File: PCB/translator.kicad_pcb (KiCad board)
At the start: 4 copper layers, 28.2 x 16 mm, 10 parts, among them J1 Conn_01x04_Pin, J2 Conn_01x04_Pin, J3 Conn_01x03_Pin, J4 Conn_01x03_Pin, SW1 SW_Push, U1 STM32G071GBU6

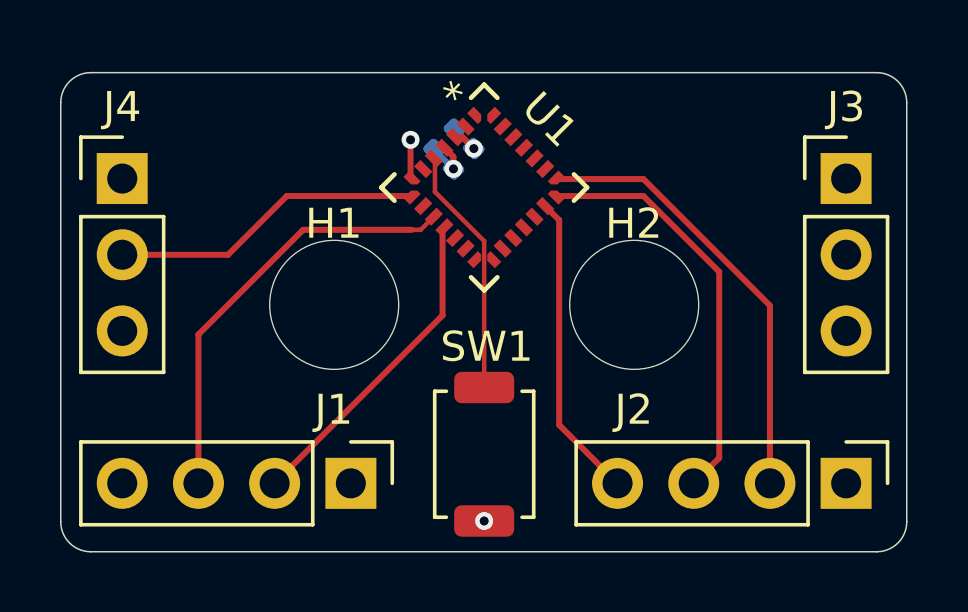
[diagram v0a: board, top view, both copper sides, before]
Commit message: reorganize and add CAD
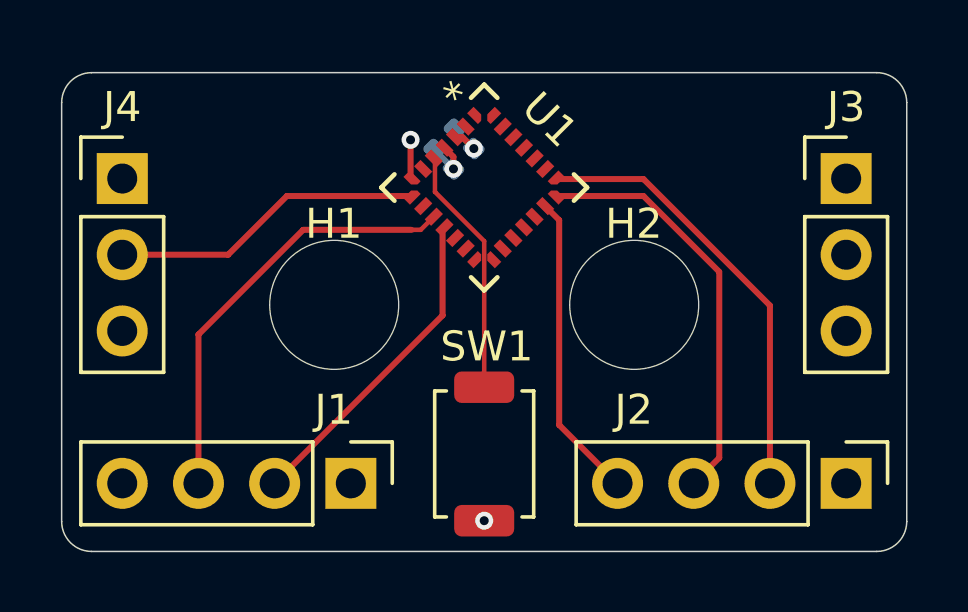
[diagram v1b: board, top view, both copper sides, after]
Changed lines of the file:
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@@
 	(footprint "Button_Switch_SMD:SW_SPST_TS-1088-xR020"
 		(layer "F.Cu")
-		(at 107.315 108.25 90)
+		(at 107.315 108.24 90)
 		(descr "SMD Tactile Switch, 3.9x3x2 mm, https://lcsc.com/datasheet/lcsc_datasheet_2504101957_XUNPU-TS-1088-AR02016_C720477.pdf")
 		(tags "Tactile Switch")
@@
 	)
 	(gr_line
-		(start 93.2 96.53)
-		(end 93.2 110.5)
+		(start 93.23 96.53)
+		(end 93.23 110.49)
 		(stroke
 			(width 0.05)
@@
 	)
 	(gr_arc
-		(start 93.2 96.53)
-		(mid 93.492893 95.822893)
-		(end 94.2 95.53)
+		(start 93.23 96.53)
+		(mid 93.522893 95.822893)
+		(end 94.23 95.53)
 		(stroke
 			(width 0.05)
@@
 	)
 	(gr_arc
-		(start 94.2 111.5)
-		(mid 93.492893 111.207107)
-		(end 93.2 110.5)
+		(start 94.23 111.49)
+		(mid 93.522893 111.197107)
+		(end 93.23 110.49)
 		(stroke
 			(width 0.05)
@@
 	(gr_line
 		(start 120.4 95.53)
-		(end 94.2 95.53)
+		(end 94.23 95.53)
 		(stroke
 			(width 0.05)
@@
 	)
 	(gr_line
-		(start 120.4 111.5)
-		(end 94.2 111.5)
+		(start 120.4 111.49)
+		(end 94.23 111.49)
 		(stroke
 			(width 0.05)
@@
 	)
 	(gr_arc
-		(start 121.4 110.5)
-		(mid 121.107107 111.207107)
-		(end 120.4 111.5)
+		(start 121.4 110.49)
+		(mid 121.107107 111.197107)
+		(end 120.4 111.49)
 		(stroke
 			(width 0.05)
@@
 	)
 	(gr_line
-		(start 121.4 110.5)
+		(start 121.4 110.49)
 		(end 121.4 96.53)
 		(stroke
@@
 	)
 	(via
-		(at 107.315 110.475)
+		(at 107.315 110.465)
 		(size 0.6)
 		(drill 0.3)
@@
 	)
 	(segment
-		(start 106.06 109.22)
-		(end 107.315 110.475)
+		(start 113.300589 98.060589)
+		(end 119.38 104.14)
 		(width 0.2)
 		(layer "In2.Cu")
@@
 	)
 	(segment
-		(start 113.300589 98.060589)
-		(end 119.38 104.14)
+		(start 109.71 108.07)
+		(end 107.315 110.465)
 		(width 0.2)
 		(layer "In2.Cu")
@@
 	)
 	(segment
-		(start 107.315 110.475)
-		(end 109.72 108.07)
+		(start 118.23 108.07)
+		(end 109.71 108.07)
 		(width 0.2)
 		(layer "In2.Cu")
@@
 	)
 	(segment
-		(start 109.72 108.07)
-		(end 118.23 108.07)
+		(start 102.87 109.22)
+		(end 97.79 104.14)
 		(width 0.2)
 		(layer "In2.Cu")
@@
 	)
 	(segment
-		(start 102.87 109.22)
-		(end 97.79 104.14)
+		(start 106.07 109.22)
+		(end 107.315 110.465)
 		(width 0.2)
 		(layer "In2.Cu")
@@
 	(segment
 		(start 102.87 109.22)
-		(end 106.06 109.22)
+		(end 106.07 109.22)
 		(width 0.2)
 		(layer "In2.Cu")
@@
 	)
 	(segment
-		(start 118.23 108.07)
-		(end 119.38 109.22)
+		(start 119.38 109.22)
+		(end 118.23 108.07)
 		(width 0.2)
 		(layer "In2.Cu")
@@
 	)
 	(segment
+		(start 107.315 101.145442)
+		(end 107.315 106.015)
+		(width 0.15)
+		(layer "F.Cu")
+		(net 10)
+	)
+	(segment
 		(start 105.672396 99.502838)
 		(end 107.315 101.145442)
 		(width 0.15)
 		(layer "F.Cu")
-		(net 10)
-	)
-	(segment
-		(start 107.315 101.145442)
-		(end 107.315 106.025)
-		(width 0.15)
-		(layer "F.Cu")

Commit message: updated connectors slightly and updated readme
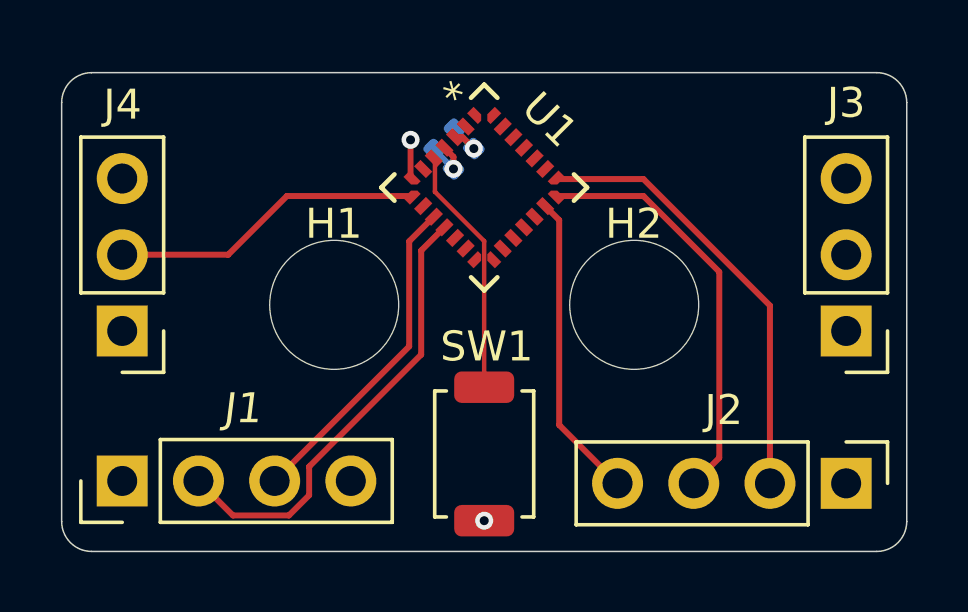
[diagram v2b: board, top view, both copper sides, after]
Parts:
- moved J1 7.62 mm to (95.2, 109.1), turned to 90 degrees
- moved J3 5.08 mm to (119.4, 104.1), turned to 180 degrees
- moved J4 5.08 mm to (95.2, 104.1), turned to 180 degrees
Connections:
- J3 pad 1: +3V3 -> GND
- J3 pad 3: GND -> +3V3
- J4 pad 1: +3V3 -> GND
- J4 pad 3: GND -> +3V3
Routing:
- net /BRK_OUT: track 10.9 -> 15.2 mm
- net /GAS_OUT: track 14.4 -> 11.0 mm
- net GND: track 49.9 -> 52.9 mm
- net +3V3: track 40.1 -> 42.2 mm
